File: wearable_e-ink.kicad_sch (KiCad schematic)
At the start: 25 parts, among them U1 4*4*1_7, U10 NPN, U3 CH340C_USB, U5 ESP-12F(ESP8266MOD), U6 TYPE-C, U7 LDO, U8 4*4*1_7, U9 NPN

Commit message: First pcb design layout
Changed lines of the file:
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@@
 	(wire
 		(pts
-			(xy 303.53 30.48) (xy 306.07 30.48)
+			(xy 304.8 30.48) (xy 306.07 30.48)
 		)
 		(stroke
@@
 	(wire
 		(pts
+			(xy 267.97 44.45) (xy 265.43 44.45)
+		)
+		(stroke
+			(width 0)
+			(type default)
+		)
+	)
+	(wire
+		(pts
 			(xy 316.23 53.34) (xy 318.77 53.34)
 		)
@@
 		(pts
 			(xy 289.56 93.98) (xy 302.26 93.98)
+		)
+		(stroke
+			(width 0)
+			(type default)
+		)
+	)
+	(wire
+		(pts
+			(xy 267.97 46.99) (xy 265.43 46.99)
 		)
 		(stroke
@@
 	)
 	(label "DTR"
-		(at 265.43 46.99 0)
+		(at 267.97 46.99 0)
 		(effects
 			(font
@@
 	)
 	(label "DTR"
-		(at 303.53 30.48 180)
+		(at 304.8 30.48 180)
 		(effects
 			(font
@@
 	)
 	(label "RTS"
-		(at 265.43 44.45 0)
-		(effects
-			(font
+		(at 267.97 44.45 0)
+		(effects
+			(font

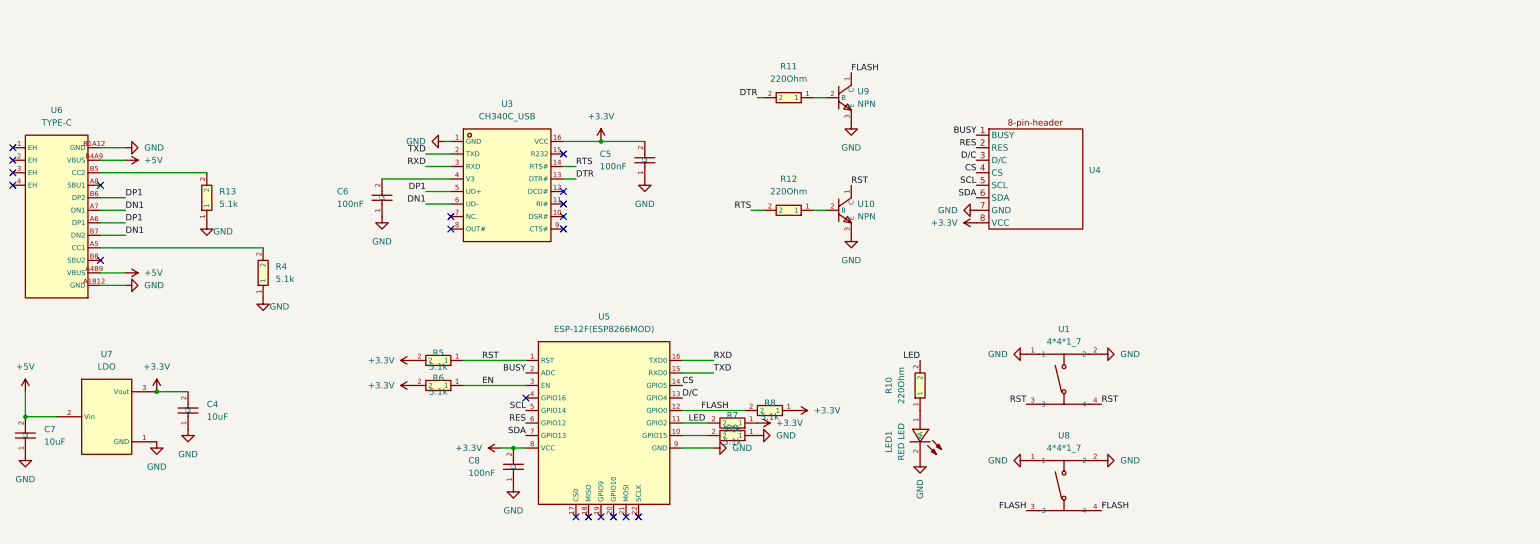
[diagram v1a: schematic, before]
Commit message: Switched out daughter board for on-board FPC and display signal conditioning. First of V2
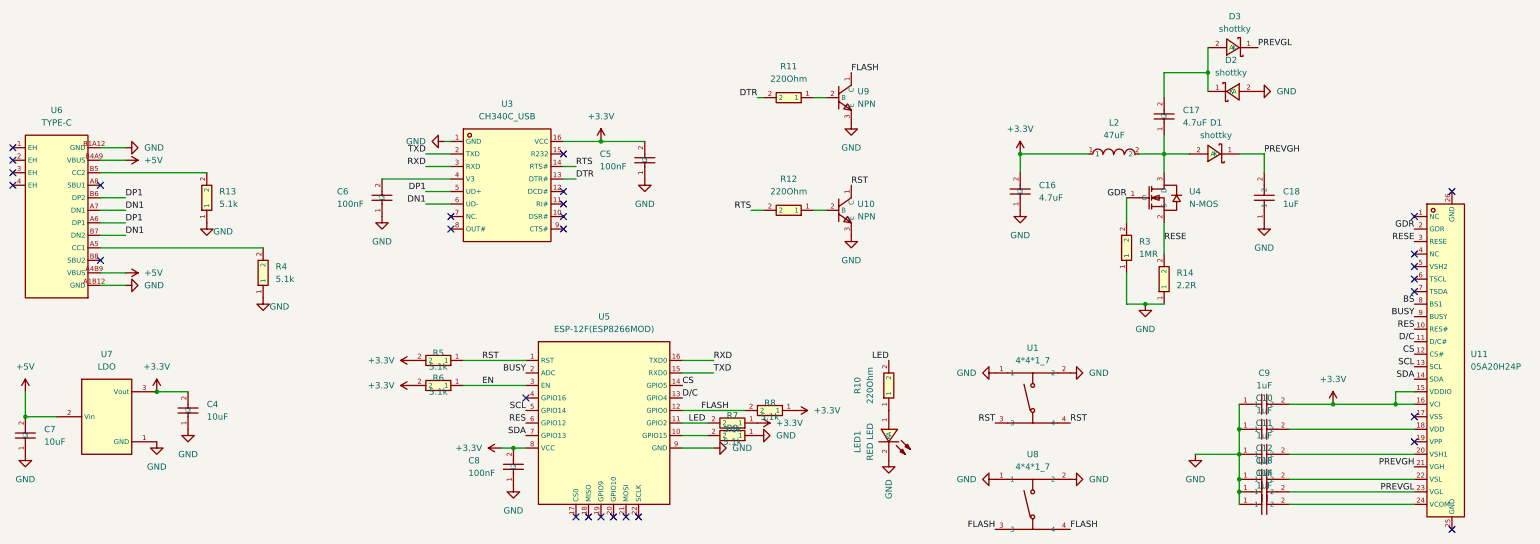
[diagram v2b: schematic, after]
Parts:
- removed U4: ~, wearable-e-inks:8pinheader, symbol wearable-e-inks:display_pin_header
- added C10, C11, C12, C13, C14, C18, C9: 1uF, wearable-e-inks:C1206, symbol wearable-e-inks:CL31B105KBHNNNE
- added C16, C17: 4.7uF, wearable-e-inks:C1206, symbol wearable-e-inks:CL31B475KAHNNNE
- added D1, D2, D3: shottky, wearable-e-inks:SOD-123_L2.8-W1.8-LS3.7-RD, symbol wearable-e-inks:LMBR0530T1G
- added L2: 47uF, wearable-e-inks:IND-SMD_L4.0-W4.0, symbol wearable-e-inks:VLS4012ET-470M
- added R14: 2.2R, wearable-e-inks:R1206, symbol wearable-e-inks:1206W4F220KT5E
- added R3: 1MR, wearable-e-inks:R1206, symbol wearable-e-inks:1206W4F1004T5E
- added U11: 05A20H24P, wearable-e-inks:FPC-SMD_24P-P0.50_05A20H24P, symbol wearable-e-inks:05A20H24P
- added U4: N-MOS, wearable-e-inks:SOT-23-LDO, symbol wearable-e-inks:IRLML2402TRPBF
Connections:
- net +3.3V: now also C16.2, C9.2, L2.1, U11.15 (VDDIO), U11.16 (VCI)
- net BUSY: now also U11.9 (BUSY)
- net CS: now also U11.12 (CS#)
- net D/C: now also U11.11 (D/C#)
- net GND: now also C10.1, C11.1, C12.1, C13.1, C14.1, C16.1, C18.1, C9.1, D2.2 (A), R14.1, R3.1
- net RES: now also U11.10 (RES#)
- net SCL: now also U11.13 (SCL)
- net SDA: now also U11.14 (SDA)
- new net: C17.2, D2.1 (K), D3.2 (A)
- new net: C17.1, D1.2 (A), L2.2, U4.3 (D)
- new net: C14.2, U11.24 (VCOM)
- new net: C10.2, U11.18 (VDD)
- new net: C12.2, U11.22 (VSL)
- new net: C11.2, U11.20 (VSH1)
- new net BS: U11.8 (BS1)
- new net GDR: R3.2, U11.2 (GDR), U4.1 (G)
- new net PREVGH: C18.2, D1.1 (K), U11.21 (VGH)
- new net PREVGL: C13.2, D3.1 (K), U11.23 (VGL)
- new net RESE: R14.2, U11.3 (RESE), U4.2 (S)
- no-connect marks 20 -> 29
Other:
- moved on the sheet: LED1, R10, U1, U8
